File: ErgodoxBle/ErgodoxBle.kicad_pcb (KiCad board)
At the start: 2 copper layers, 182.8 x 158.9 mm, 154 parts, among them SW0:10 SW0:3, SW0:11 SW0:2, SW0:12 SW0:1, SW0:7 SW0:6, SW0:8 SW0:5, SW0:9 SW0:4, SW1:10 SW1:3, SW1:11 SW1:2, SW1:12 SW1:1, SW1:13 SW1:0, SW1:9 SW1:4, SW2:10 SW2:3, SW2:11 SW2:2, SW2:12 SW2:1, SW2:13 SW2:0, SW2:7 SW2:6, SW2:8 SW2:5, SW2:9 SW2:4, SW3:10 SW3:3, SW3:11 SW3:2, SW3:12 SW3:1, SW3:13 SW3:0, SW3:8 SW3:5, SW3:9 SW3:4, SW4:10 SW4:3, SW4:11 SW4:2, SW4:12 SW4:1, SW4:13 SW4:0, SW4:7 SW4:6, SW4:8 SW4:5, SW4:9 SW4:4, SW5:10 SW5:3, SW5:11 SW5:2, SW5:12 SW5:1, SW5:13 SW5:0, SW5:7 SW5:6, SW5:8 SW5:5, SW5:9 SW5:4

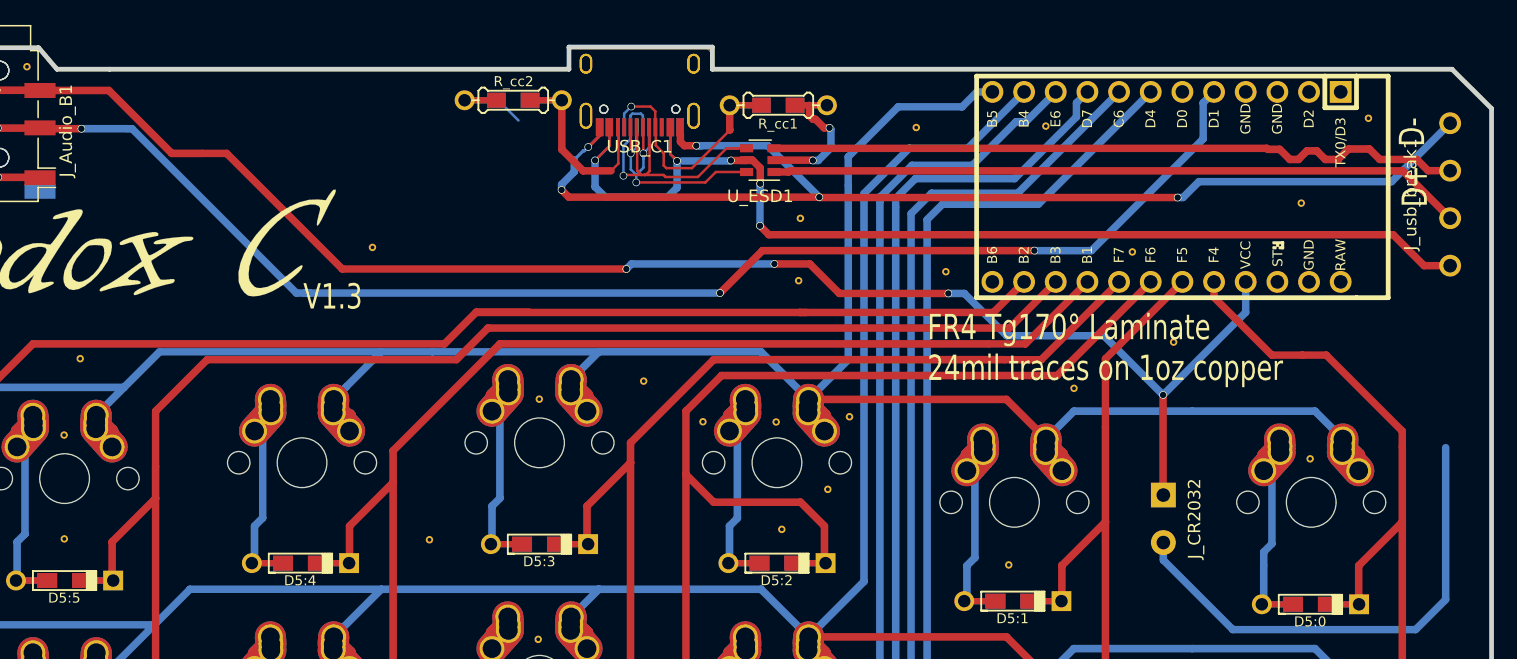
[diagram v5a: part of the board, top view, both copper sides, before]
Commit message: align front and back usb c port
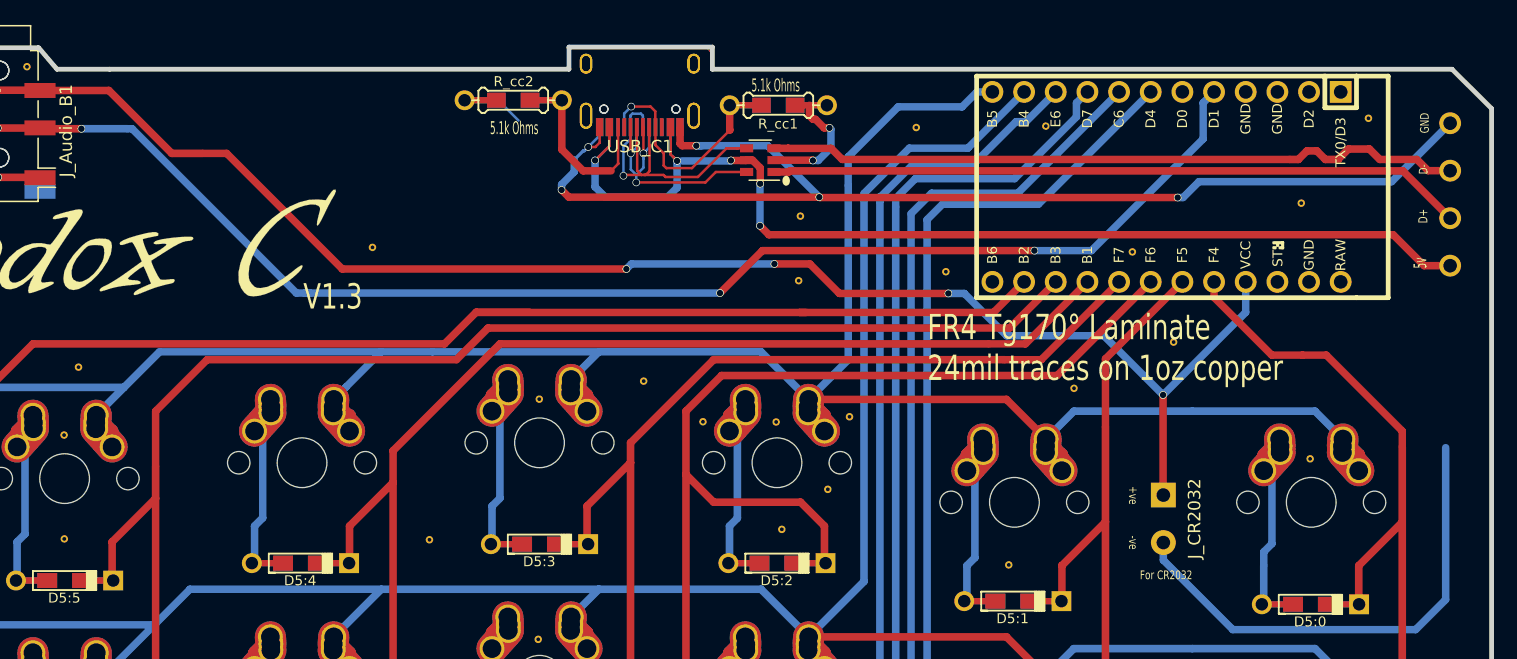
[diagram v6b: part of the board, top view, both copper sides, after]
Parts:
- moved REF** 0.69 mm to (92.6, 56.2)
- moved REF** 0.18 mm to (150.5, 44.0)
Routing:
- net /GND_USB: track 98.5 -> 100.0 mm
- net /D_IN+: track 21.4 -> 22.5 mm
- net /VUSB: track 91.3 -> 92.0 mm
- net /CC1: track 16.7 -> 17.3 mm
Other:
- board text added: "+ve"
- board text added: "-ve"
- board text added: "5.1k Ohms"
- board text added: "5v"
- board text added: "For CR2032"
- board text added: "GND"
- board text added: "•"

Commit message: redo fill zone
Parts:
- removed the REF** at (150.5, 44.0)
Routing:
- net /GND_USB: track 100.0 -> 101.1 mm
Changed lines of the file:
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@@
     (thickness 1.6002)
     (drawings 48)
-    (tracks 1125)
+    (tracks 1126)
     (zones 0)
-    (modules 154)
+    (modules 153)
     (nets 80)
   )
@@
   )
   (module usbc_footprint:via-0.6mm (layer Front)
-    (at 150.4696 44.0436)
-    (fp_text reference REF** (at 0 1.27) (layer F.SilkS) hide
-      (effects (font (size 1 1) (thickness 0.15)))
-    )
-    (fp_text value via-0.6mm (at 0 -1.27) (layer F.Fab) hide
-      (effects (font (size 1 1) (thickness 0.15)))
-    )
-    (pad 1 thru_hole circle (at 0 0) (size 0.6 0.6) (drill 0.3) (layers *.Cu)
-      (net 54 GND) (zone_connect 2))
-  )
-  (module usbc_footprint:via-0.6mm (layer Front)
     (at 196.04228 36.195)
     (fp_text reference REF** (at 0 1.27) (layer F.SilkS) hide
@@
   (segment (start 151.98598 42.52214) (end 147.85848 38.39464) (width 0.6) (layer Back) (net 72))
   (via (at 131.31038 41.94302) (size 0.6096) (drill 0.508) (layers Front Back) (net 72))
-  (segment (start 151.98598 42.52214) (end 131.8895 42.52214) (width 0.6) (layer Front) (net 72))
-  (segment (start 131.8895 42.52214) (end 131.31038 41.94302) (width 0.6) (layer Front) (net 72))
   (segment (start 131.31038 41.511968) (end 132.31876 40.503588) (width 0.6) (layer Back) (net 72))
   (segment (start 131.31038 41.94302) (end 131.31038 41.511968) (width 0.6) (layer Back) (net 72))
@@
   (segment (start 134.3668 38.15) (end 134.3668 36.905) (width 0.2032) (layer Front) (net 72))
   (segment (start 134.01802 38.49878) (end 134.3668 38.15) (width 0.2032) (layer Front) (net 72))
+  (segment (start 131.31038 41.94302) (end 133.28396 43.9166) (width 0.6) (layer Front) (net 72))
+  (segment (start 150.59152 43.9166) (end 151.98598 42.52214) (width 0.6) (layer Front) (net 72))
+  (segment (start 133.28396 43.9166) (end 150.59152 43.9166) (width 0.6) (layer Front) (net 72))
   (segment (start 137.3759 40.39108) (end 137.3759 38.3753) (width 0.2032) (layer Front) (net 73))
   (segment (start 138.3672 38.3666) (end 138.37158 38.37098) (width 0.2032) (layer Front) (net 73))

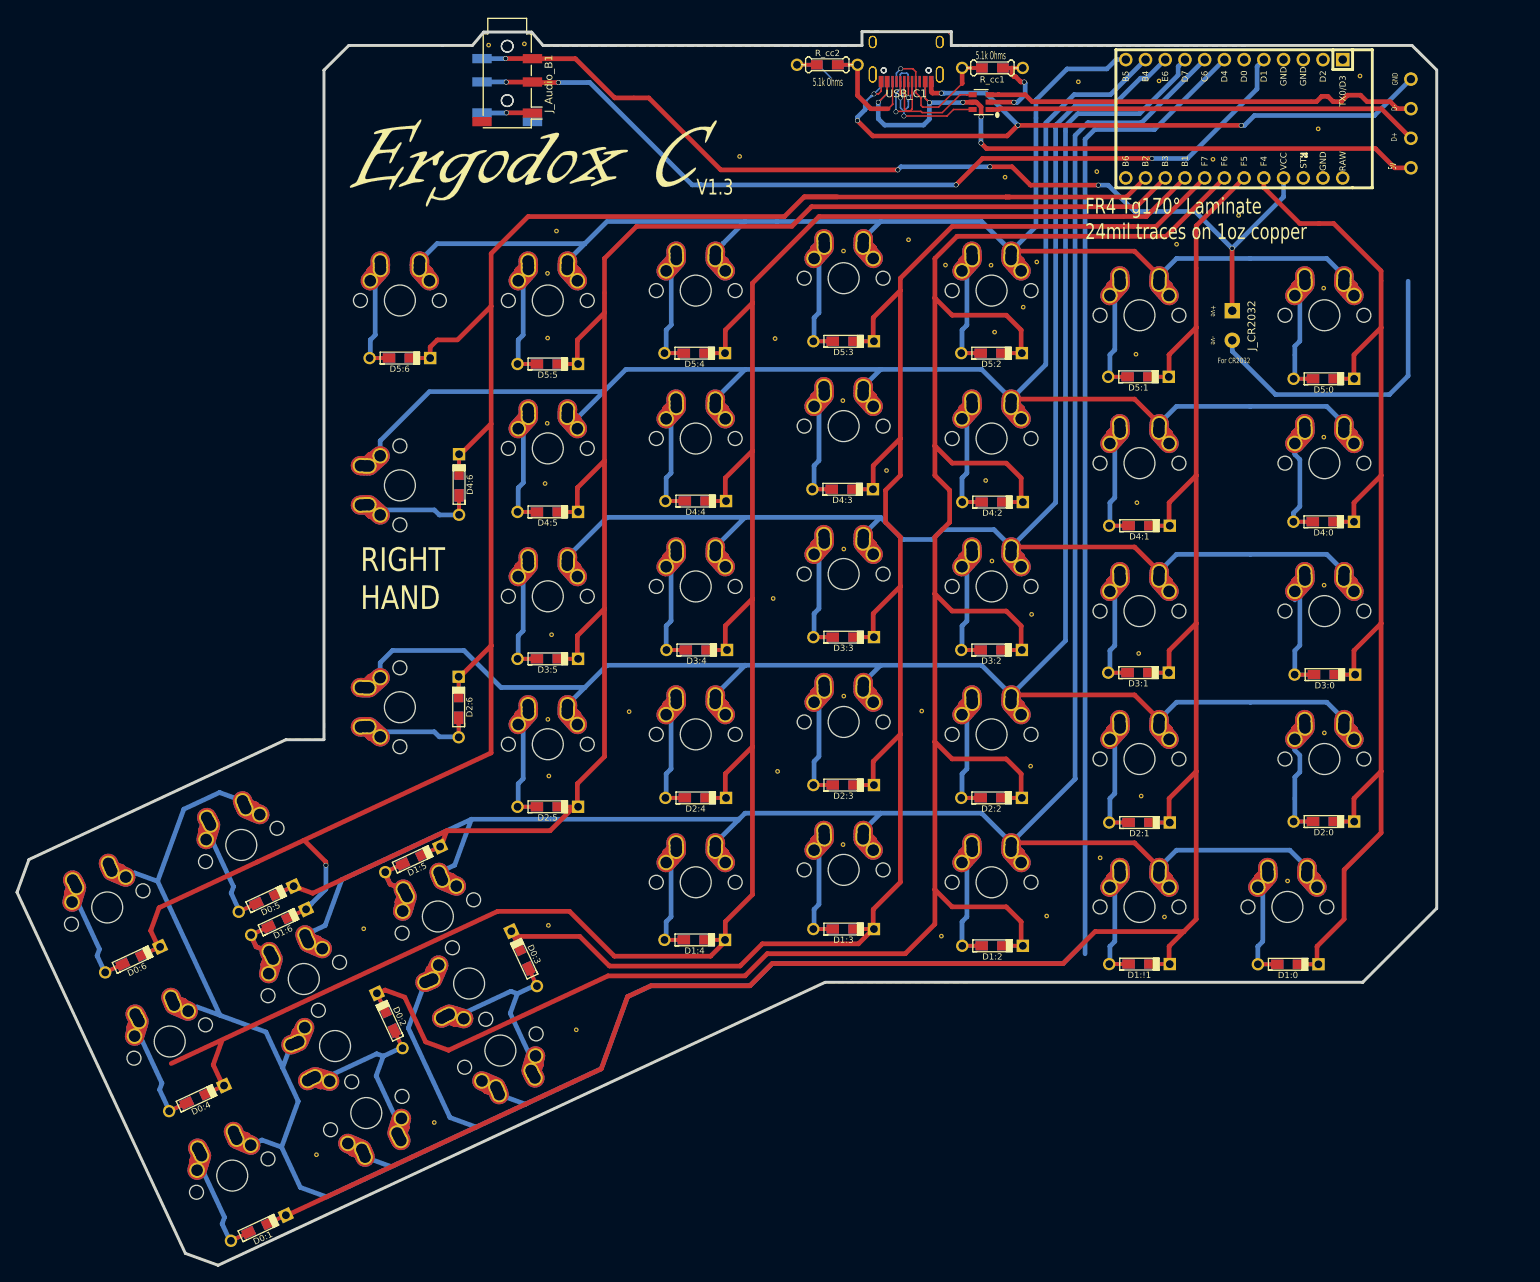
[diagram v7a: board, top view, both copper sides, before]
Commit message: added svg for case
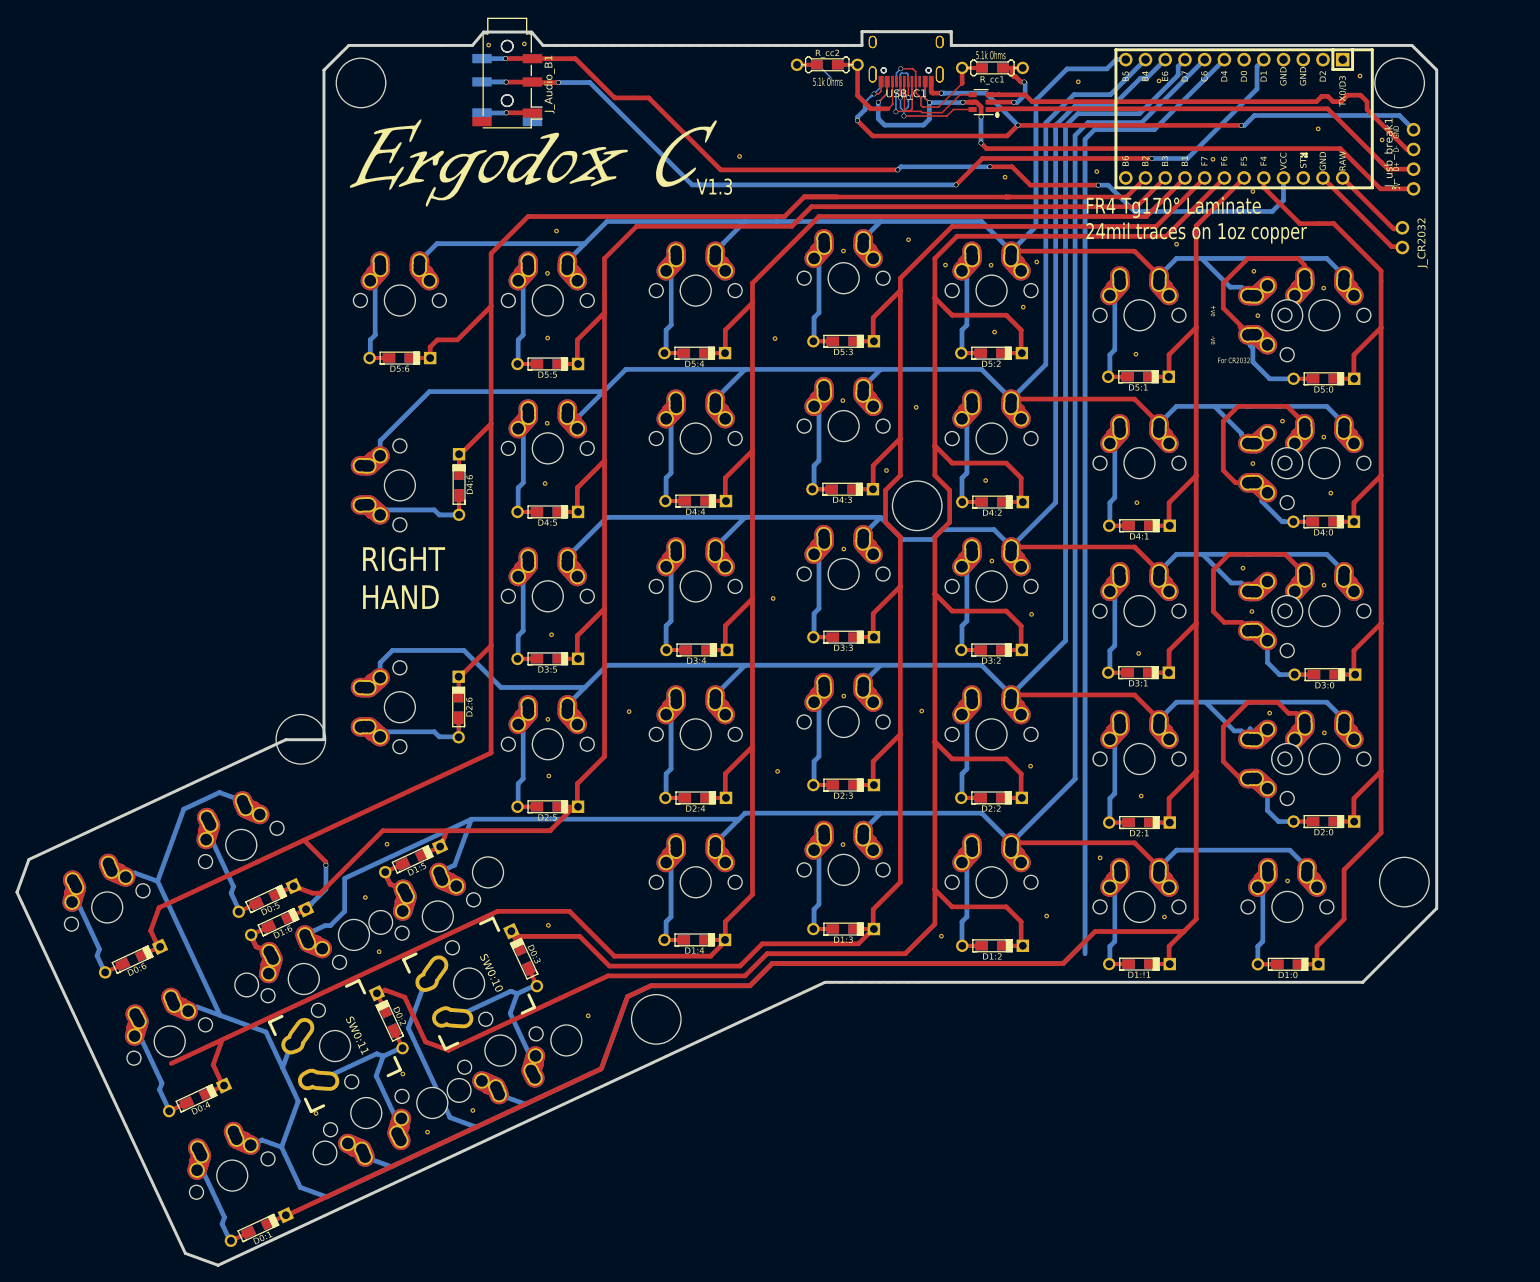
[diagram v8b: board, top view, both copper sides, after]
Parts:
- added REF**: via-0.6mm, usbc_footprint:via-0.6mm, F.Cu at (201.7, 140.0)
- added REF**: via-0.6mm, usbc_footprint:via-0.6mm, F.Cu at (105.3, 157.7)
- added REF**: via-0.6mm, usbc_footprint:via-0.6mm, F.Cu at (59.6, 121.6)
- added REF**: via-0.6mm, usbc_footprint:via-0.6mm, F.Cu at (138.9, 91.5)
- added REF**: via-0.6mm, usbc_footprint:via-0.6mm, F.Cu at (201.1, 37.1)
- added REF**: via-0.6mm, usbc_footprint:via-0.6mm, F.Cu at (81.8, 169.4)
- added REF**: via-0.6mm, usbc_footprint:via-0.6mm, F.Cu at (182.4, 61.3)
- added REF**: via-0.6mm, usbc_footprint:via-0.6mm, F.Cu at (186.1, 80.6)
- added REF**: via-0.6mm, usbc_footprint:via-0.6mm, F.Cu at (184.4, 118.2)
- added REF**: via-0.6mm, usbc_footprint:via-0.6mm, F.Cu at (67.9, 142.0)
- added REF**: via-0.6mm, usbc_footprint:via-0.6mm, F.Cu at (182.9, 67.1)
- added REF**: via-0.6mm, usbc_footprint:via-0.6mm, F.Cu at (192.3, 89.9)
- added REF**: via-0.6mm, usbc_footprint:via-0.6mm, F.Cu at (182.1, 105.2)
- added REF**: via-0.6mm, usbc_footprint:via-0.6mm, F.Cu at (182.2, 86.1)
- added REF**: via-0.6mm, usbc_footprint:via-0.6mm, F.Cu at (181.0, 99.6)
- added REF**: via-0.6mm, usbc_footprint:via-0.6mm, F.Cu at (69.7, 149.0)
- added REF**: via-0.6mm, usbc_footprint:via-0.6mm, F.Cu at (61.6, 169.8)
- added REF**: via-0.6mm, usbc_footprint:via-0.6mm, F.Cu at (72.8, 164.7)
- added REF**: via-0.6mm, usbc_footprint:via-0.6mm, F.Cu at (70.7, 135.1)
- added REF**: via-0.6mm, usbc_footprint:via-0.6mm, F.Cu at (67.3, 37.1)
- added REF**: via-0.6mm, usbc_footprint:via-0.6mm, F.Cu at (138.9, 78.9)
- added REF**: via-0.6mm, usbc_footprint:via-0.6mm, F.Cu at (198.9, 44.4)
- J_CR2032: footprint Connector_Wire:SolderWirePad_1x02_P3.81mm_Drill0.8mm -> usbc_footprint:Custom_SolderWirePad_1x02_P1.75mm_Drill1.09mm
- J_usb_break1: footprint Connector_Wire:SolderWirePad_1x04_P3.81mm_Drill1mm -> usbc_footprint:Custom_SolderWirePad_1x04_P1.7526mm_Drill1.0922mm
- SW0:10, SW0:11: footprint Keebio-Parts:Hybrid_PCB_100H_Dual_hole -> Keebio-Parts:Hybrid_PCB_200H-dual
- SW2:13, SW3:13, SW4:13, SW5:13: footprint Keebio-Parts:Hybrid_PCB_100H_Dual_hole -> usbc_footprint:correct_Hybrid_PCB_100v_150H_Dual_hole
- moved J_CR2032 24.4 mm to (201.5, 55.7)
- moved J_usb_break1 3.74 mm to (202.9, 51.7)
- moved REF** 3.60 mm to (182.2, 51.1)
- moved REF** 2.37 mm to (96.6, 157.2)
- moved REF** 1.52 mm to (75.9, 172.2)
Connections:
- J_CR2032 pad 1: /Vcc -> /RAW
- proMicro1 pad 23: Net-(proMicro1-Pad23) -> GND
- proMicro1 pad 24: Net-(proMicro1-Pad24) -> /RAW
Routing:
- net GND: track 58.0 -> 32.1 mm
- net Net-(D3:0-Pad2): track 18.9 -> 40.9 mm
- net Net-(D5:0-Pad2): track 17.8 -> 39.7 mm
- net Net-(D4:0-Pad2): track 18.4 -> 39.6 mm
- net Net-(D2:0-Pad2): track 18.4 -> 38.2 mm
- net /Vcc: track 126.9 -> 115.2 mm, vias 5 -> 4
- net /RAW: track 0.00 -> 10.2 mm
- net /ROW2: track 285.0 -> 294.1 mm
- net /ROW3: track 227.6 -> 236.0 mm
- net /ROW5: track 211.5 -> 219.7 mm
- net /ROW4: track 245.4 -> 252.6 mm
- net /D-: track 56.3 -> 59.4 mm
- net /D+: track 55.9 -> 57.8 mm
- net /COL5: track 213.3 -> 214.8 mm
- net /VUSB: track 92.0 -> 93.4 mm
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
